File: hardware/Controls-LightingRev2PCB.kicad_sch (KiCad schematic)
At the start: 39 parts, among them IC2 TLV70433DBVT, J3 53307-2471, J4 Conn_02x08_Top_Bottom, Q2 IRLML0030, Q3 IRLML0030, U1 TLV2371DBV, U2 INA241A5xD, U3 INA241A5xD, U4 INA241A5xD, U5 SN74LV1T34DBV, U8 TLV2371DBV, U9 TLV2371DBV

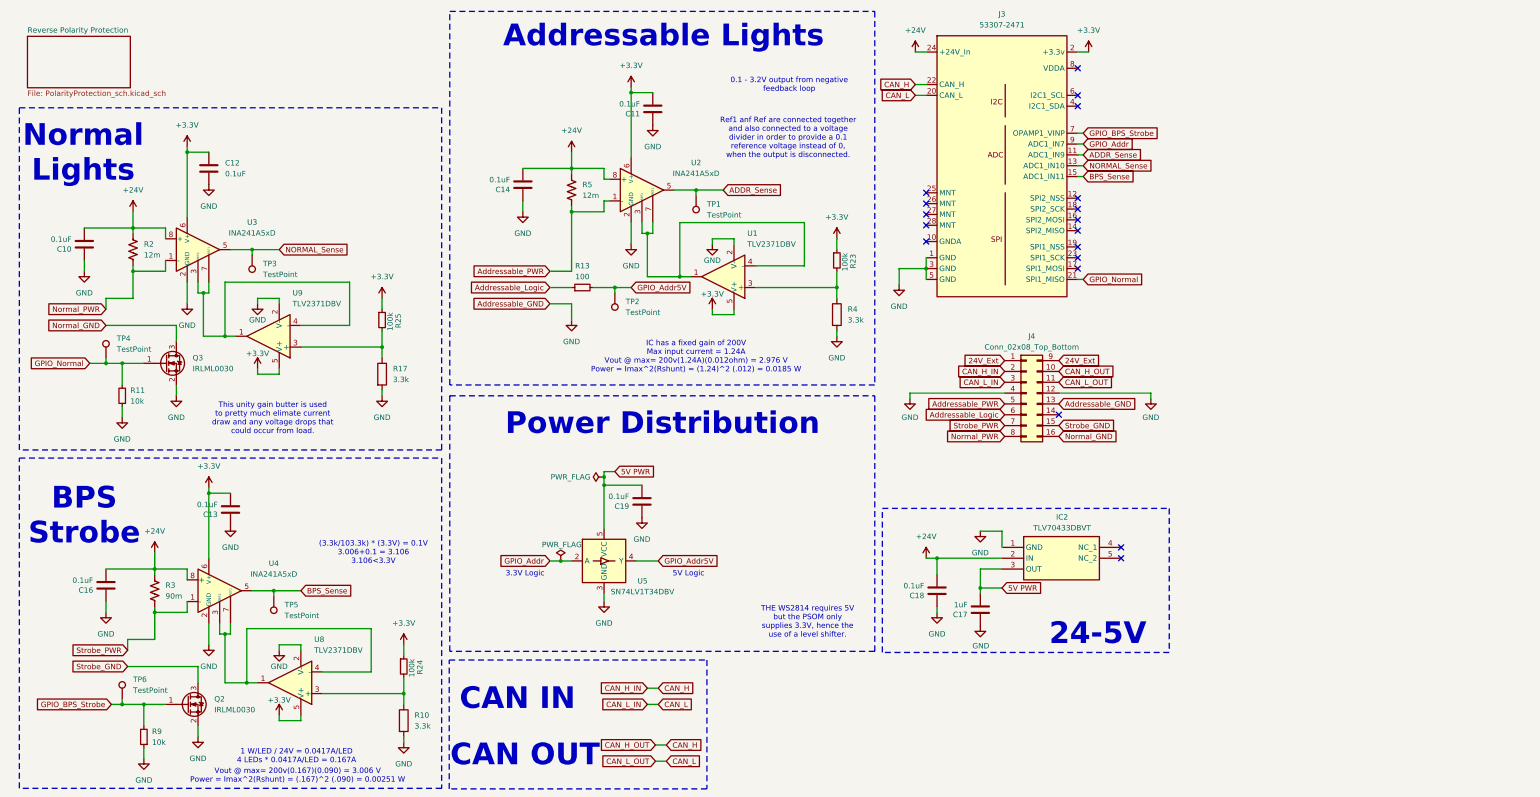
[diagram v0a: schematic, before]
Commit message: Routed but having issues with gnd being pretty isolated
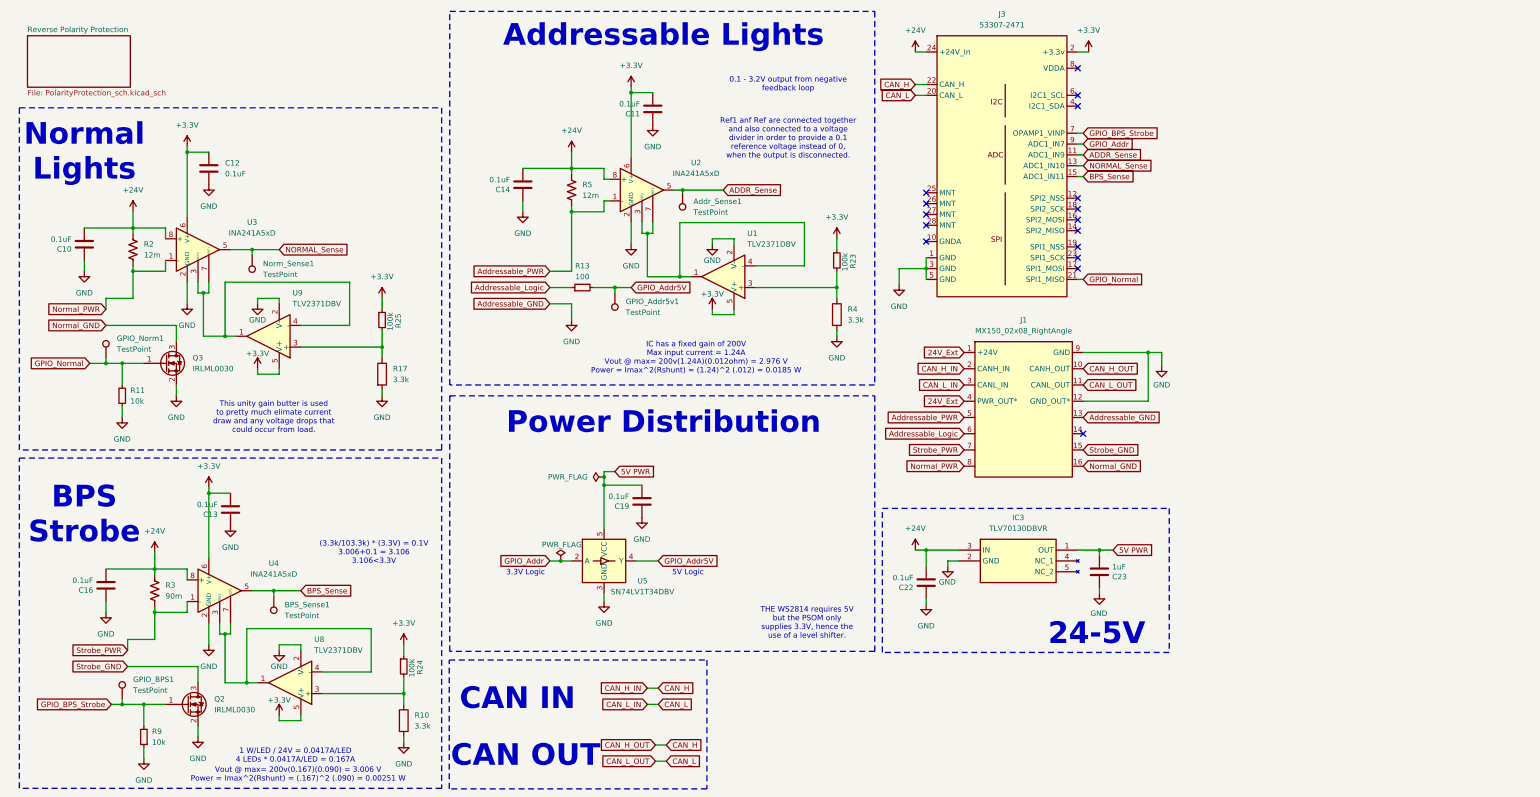
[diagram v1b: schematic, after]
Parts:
- removed C17: 1uF, Capacitor_SMD:C_0603_1608Metric, symbol Device:C
- removed C18: 0.1uF, Capacitor_SMD:C_0603_1608Metric, symbol Device:C
- removed IC2: TLV70433DBVT, SOT95P280X145-5N, symbol Misc:TLV70433DBVT
- removed J4: Conn_02x08_Top_Bottom, MX150:CONN_SD-75900-001_2X08_MOL, symbol Connector_Generic:Conn_02x08_Top_Bottom
- added C22: 0.1uF, Capacitor_SMD:C_0603_1608Metric, symbol Device:C
- added C23: 1uF, Capacitor_SMD:C_0603_1608Metric, symbol Device:C
- added IC3: TLV70130DBVR, UTSVT_Power:TLV70130DBVR, symbol UTSVT-Power:TLV70130DBVR
- added J1: MX150_02x08_RightAngle, UTSVT_Connectors:CONN_SD-75900-001_2X08_MOL, symbol UTSVT-Connectors:MX150_02x08_RightAngle
- R2, R3, R5: footprint Resistor_SMD:R_0603_1608Metric -> Resistor_SMD:R_1206_3216Metric_Pad1.30x1.75mm_HandSolder
- renumbered TP1 to Addr_Sense1, TP5 to BPS_Sense1, TP2 to GPIO_Addr5v1, TP6 to GPIO_BPS1, TP4 to GPIO_Norm1, TP3 to Norm_Sense1
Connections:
- net +24V: now also C22.2, IC3.3 (IN)
- net 24V_Ext: now also J1.1 (+24V), J1.4 (PWR_OUT*)
- net 5V PWR: now also C23.2, IC3.1 (OUT)
- net Addressable_Logic: now also J1.6
- net Addressable_PWR: now also J1.5
- net CAN_H: now also J1.10 (CANH_OUT), J1.2 (CANH_IN)
- net CAN_L: now also J1.11 (CANL_OUT), J1.3 (CANL_IN)
- net GND: now also C22.1, C23.1, IC3.2 (GND), J1.12 (GND_OUT*), J1.13, J1.9 (GND)
- net Normal_GND: now also J1.16
- net Normal_PWR: now also J1.8
- net Strobe_GND: now also J1.15
- net Strobe_PWR: now also J1.7
- no-connect marks 18 -> 16
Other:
- moved on the sheet: Addr_Sense1

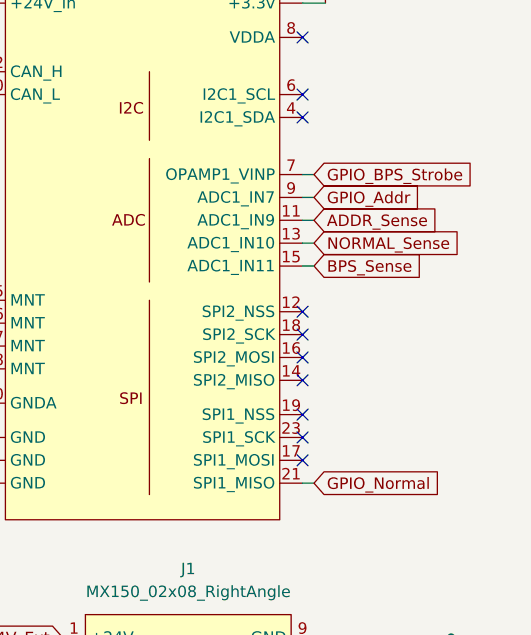
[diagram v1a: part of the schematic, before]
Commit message: Test points added
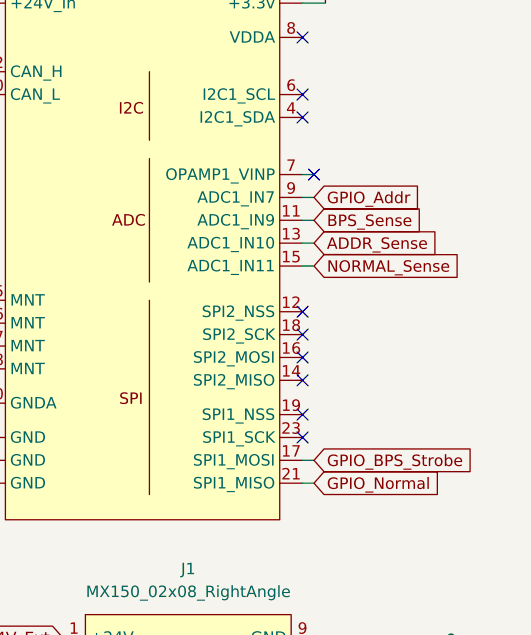
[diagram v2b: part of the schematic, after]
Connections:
- net ADDR_Sense: now also J3.13 (ADC1_IN10); no longer J3.11 (ADC1_IN9)
- net BPS_Sense: now also J3.11 (ADC1_IN9); no longer J3.15 (ADC1_IN11)
- net GPIO_BPS_Strobe: now also J3.17 (SPI1_MOSI); no longer J3.7 (OPAMP1_VINP)
- net NORMAL_Sense: now also J3.15 (ADC1_IN11); no longer J3.13 (ADC1_IN10)

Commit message: BOM
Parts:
- C12: P/N (none) -> MLASH168SB7104KTNA01
- C22: P/N MLASU168SB5105KTNA01 -> MLASH168SB7104KTNA01
- Q2, Q3: P/N (none) -> IRLML0030TRPBF
- R10, R17, R4: P/N (none) -> ERJ-S03D3301V
- R11, R9: P/N CRCW080510K0FKEAC -> CRCW060310K0FKEI
- R13: value 100 -> 100k; P/N SDR10EZPF1001 -> CRCW0603100KFKEE
- R2, R5: P/N (none) -> RLC73PV2ER012FTDF
- R23, R24, R25: P/N CRCW0805100KFKEAC -> CRCW0603100KFKEE
- R3: P/N (none) -> ERJ-L14UF90MU
- U1, U8, U9: P/N (none) -> TLV2371IDBVR
- U2, U3, U4: P/N (none) -> INA241A5QDRQ1
- U5: P/N (none) -> SN74LV1T34DBVR
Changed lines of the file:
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@@
 			)
 		)
-		(property "Description" ""
+		(property "Description" "Thick Film Resistors - SMD 100K OHM 1%"
 			(at 104.14 167.64 0)
 			(effects
@@
 			)
 		)
-		(property "P/N" "CRCW0805100KFKEAC"
+		(property "P/N" "CRCW0603100KFKEE"
 			(at 104.14 167.64 0)
 			(effects
@@
 			)
 		)
-		(property "Description" "Unpolarized capacitor"
+		(property "Description" "Multilayer Ceramic Capacitors MLCC - SMD/SMT 100V 0.1uF X7R 0603 10% Medical"
 			(at 132.08 54.61 0)
 			(effects
@@
 			)
 		)
-		(property "Description" "Unpolarized capacitor"
+		(property "Description" "Multilayer Ceramic Capacitors MLCC - SMD/SMT 100V 0.1uF X7R 0603 10% Medical"
 			(at 29.21 68.58 0)
 			(effects
@@
 			)
 		)
-		(property "Description" "Resistor"
+		(property "Description" "Thick Film Resistors - SMD 0603 0.5% 3.3kOhm Anti-Sulfur AEC-Q200"
 			(at 205.74 85.09 0)
 			(effects
@@
 			)
 		)
+		(property "P/N" "ERJ-S03D3301V"
+			(at 205.74 85.09 0)
+			(effects
+				(font
+					(size 1.27 1.27)
+				)
+			)
+		)
 		(pin "2"
 		)
@@
 			)
 		)
-		(property "Description" "Rail-to-Rail Input/Output Operational Amplifier, SOT-23-5"
+		(property "Description" "Operational Amplifiers - Op Amps 550uA/Ch 3MHz R/R Op A 595-TLV2371IDBVT"
 			(at 179.07 76.2 0)
 			(effects
@@
 			)
 		)
+		(property "P/N" "TLV2371IDBVR"
+			(at 179.07 76.2 0)
+			(effects
+				(font
+					(size 1.27 1.27)
+				)
+			)
+		)
 		(pin "5"
 		)
@@
 			)
 		)
-		(property "Description" ""
+		(property "Description" "Thick Film Resistors - SMD 10K OHM 1%"
 			(at 43.18 184.15 0)
 			(effects
@@
 			)
 		)
-		(property "P/N" "CRCW080510K0FKEAC"
+		(property "P/N" "CRCW060310K0FKEI "
 			(at 43.18 184.15 0)
 			(effects
@@
 			)
 		)
-		(property "Description" ""
+		(property "Description" "Thick Film Resistors - SMD 10K OHM 1%"
 			(at 38.1 104.14 0)
 			(effects
@@
 			)
 		)
-		(property "P/N" "CRCW080510K0FKEAC"
+		(property "P/N" "CRCW060310K0FKEI "
 			(at 38.1 104.14 0)
 			(effects
@@
 			)
 		)
-		(property "Description" "Unpolarized capacitor"
+		(property "Description" "Multilayer Ceramic Capacitors MLCC - SMD/SMT 100V 0.1uF X7R 0603 10% Medical"
 			(at 162.56 36.83 0)
 			(effects
@@
 			)
 		)
-		(property "Description" "Unpolarized capacitor"
+		(property "Description" "Multilayer Ceramic Capacitors MLCC - SMD/SMT 100V 0.1uF X7R 0603 10% Medical"
 			(at 226.695 147.955 0)
 			(effects
@@
 			)
 		)
-		(property "P/N" "MLASU168SB5105KTNA01"
+		(property "P/N" "MLASH168SB7104KTNA01"
 			(at 226.695 147.955 0)
 			(effects
@@
 			)
 		)
-		(property "Description" "Unpolarized capacitor"
+		(property "Description" "Multilayer Ceramic Capacitors MLCC - SMD/SMT 50V 1uF X5R 0603 10%"
 			(at 267.335 145.415 0)
 			(effects
@@
 			)
 		)
-		(property "Description" "Resistor, US symbol"
+		(property "Description" "Current Sense Resistors - SMD 1210 90mOhm 1% Curr Sense AEC-Q200"
 			(at 45.72 149.86 0)
 			(effects
@@
 			)
 		)
+		(property "P/N" "ERJ-L14UF90MU"
+			(at 45.72 149.86 0)
+			(effects
+				(font
+					(size 1.27 1.27)
+				)
+			)
+		)
 		(pin "1"
 		)
@@
 			)
 		)
-		(property "Value" "100"
+		(property "Value" "100k"
 			(at 146.05 76.2 90)
 			(effects
@@
 			)
 		)
-		(property "Description" ""
+		(property "Description" "Thick Film Resistors - SMD 100K OHM 1%"
 			(at 146.05 78.74 0)
 			(effects
@@
 			)
 		)
-		(property "P/N" "SDR10EZPF1001"
+		(property "P/N" "CRCW0603100KFKEE"
 			(at 146.05 78.74 0)
 			(effects
@@
 			)
 		)
-		(property "Description" "Resistor"
+		(property "Description" "Thick Film Resistors - SMD 0603 0.5% 3.3kOhm Anti-Sulfur AEC-Q200"
 			(at 99.06 99.06 0)
 			(effects
@@
 			)
 		)
+		(property "P/N" "ERJ-S03D3301V"
+			(at 99.06 99.06 0)
+			(effects
+				(font
+					(size 1.27 1.27)
+				)
+			)
+		)
 		(pin "2"
 		)
@@
 			)
 		)
-		(property "Description" "5.3A Id, 30V Vds, 27mOhm Rds, N-Channel HEXFET Power MOSFET, SOT-23"
+		(property "Description" "MOSFETs MOSFT 30V 5.2A 28mOhm 3.6nC Qg"
 			(at 48.26 96.52 0)
 			(effects
@@
 			)
 		)
+		(property "P/N" "IRLML0030TRPBF"
+			(at 48.26 96.52 0)
+			(effects
+				(font
+					(size 1.27 1.27)
+				)
+			)
+		)
 		(pin "1"
 		)
@@
 			)
 		)
-		(property "Description" ""
+		(property "Description" "Thick Film Resistors - SMD 100K OHM 1%"
 			(at 99.06 86.36 0)
 			(effects
@@
 			)
 		)
-		(property "P/N" "CRCW0805100KFKEAC"
+		(property "P/N" "CRCW0603100KFKEE"
 			(at 99.06 86.36 0)
 			(effects
@@
 			)
 		)
-		(property "Description" "Resistor, US symbol"
+		(property "Description" "Current Sense Resistors - SMD RLC73PV 2E R012 1% 1K RL"
 			(at 40.64 69.85 0)
 			(effects
@@
 			)
 		)
+		(property "P/N" "RLC73PV2ER012FTDF"
+			(at 40.64 69.85 0)
+			(effects
+				(font
+					(size 1.27 1.27)
+				)
+			)
+		)
 		(pin "1"
 		)
@@
 			)
 		)
-		(property "Description" "Unpolarized capacitor"
+		(property "Description" "Multilayer Ceramic Capacitors MLCC - SMD/SMT 100V 0.1uF X7R 0603 10% Medical"
 			(at 34.29 148.59 0)
 			(effects
@@
 			)
 		)
-		(property "Description" "Resistor, US symbol"
+		(property "Description" "Current Sense Resistors - SMD RLC73PV 2E R012 1% 1K RL"
 			(at 143.51 55.88 0)
 			(effects
@@
 			)
 		)
+		(property "P/N" "RLC73PV2ER012FTDF"
+			(at 143.51 55.88 0)
+			(effects
+				(font
+					(size 1.27 1.27)
+				)
+			)
+		)
 		(pin "1"
 		)
@@
 			)
 		)
-		(property "Description" ""
+		(property "Description" "Thick Film Resistors - SMD 100K OHM 1%"
 			(at 205.74 72.39 0)
 			(effects
@@
 			)
 		)
-		(property "P/N" "CRCW0805100KFKEAC"
+		(property "P/N" "CRCW0603100KFKEE"
 			(at 205.74 72.39 0)
 			(effects
@@
 			)
 		)
-		(property "Description" "Unpolarized capacitor"
+		(property "Description" "Multilayer Ceramic Capacitors MLCC - SMD/SMT 100V 0.1uF X7R 0603 10% Medical"
 			(at 160.02 128.905 0)
 			(effects
@@
 			)
 		)
-		(property "Description" "Rail-to-Rail Input/Output Operational Amplifier, SOT-23-5"
+		(property "Description" "Operational Amplifiers - Op Amps 550uA/Ch 3MHz R/R Op A 595-TLV2371IDBVT"
 			(at 77.47 171.45 0)
 			(effects
@@
 			)
 		)
+		(property "P/N" "TLV2371IDBVR"
+			(at 77.47 171.45 0)
+			(effects
+				(font
+					(size 1.27 1.27)
+				)
+			)
+		)
 		(pin "5"
 		)
@@
 			)
 		)
-		(property "Description" "High- and Low-Side, Bidirectional, Zero-Drift, Current-Sense Amplifier With Enhanced PWM Rejection, 200V/V, ±0.01% Gain Accuracy, ±10 μV Offset Voltage, SOIC-8"
+		(property "Description" "Current Sense Amplifiers AEC-Q100 -4V to 110 V bidirectional ultr"
 			(at 160.02 55.88 0)
 			(effects
@@
 			)
 		)
+		(property "P/N" "INA241A5QDRQ1"
+			(at 160.02 55.88 0)
+			(effects
+				(font
+					(size 1.27 1.27)
+				)
+			)
+		)
 		(pin "1"
 		)
@@
 			)
 		)
-		(property "Description" "Unpolarized capacitor"
+		(property "Description" "Multilayer Ceramic Capacitors MLCC - SMD/SMT 100V 0.1uF X7R 0603 10% Medical"
 			(at 63.5 130.81 0)
 			(effects
@@
 			)
 		)
-		(property "Description" "Single Power Supply, Single Buffer GATE, CMOS Logic, Level Shifter, SOT-23-5"
+		(property "Description" "Translation - Voltage Levels SGL Pwr Spply Buffer GATE CMOS"
 			(at 151.13 142.875 0)
 			(effects
@@
 			)
 		)
+		(property "P/N" "SN74LV1T34DBVR"
+			(at 151.13 142.875 0)
+			(effects
+				(font
+					(size 1.27 1.27)
+				)
+			)
+		)
 		(pin "2"
 		)
@@
 			)
 		)
-		(property "Description" "Unpolarized capacitor"
+		(property "Description" "Multilayer Ceramic Capacitors MLCC - SMD/SMT 100V 0.1uF X7R 0603 10% Medical"
 			(at 58.42 50.8 0)
 			(effects
@@
 			)
 		)
+		(property "P/N" "MLASH168SB7104KTNA01"
+			(at 58.42 50.8 0)
+			(effects
+				(font
+					(size 1.27 1.27)
+				)
+			)
+		)
 		(pin "1"
 		)
@@
 			)
 		)
-		(property "Description" "High- and Low-Side, Bidirectional, Zero-Drift, Current-Sense Amplifier With Enhanced PWM Rejection, 200V/V, ±0.01% Gain Accuracy, ±10 μV Offset Voltage, SOIC-8"
+		(property "Description" "Current Sense Amplifiers AEC-Q100 -4V to 110 V bidirectional ultr"
 			(at 55.88 69.85 0)
 			(effects
@@
 			)
 		)
+		(property "P/N" "INA241A5QDRQ1"
+			(at 55.88 69.85 0)
+			(effects
+				(font
+					(size 1.27 1.27)
+				)
+			)
+		)
 		(pin "1"
 		)
@@
 			)
 		)
-		(property "Description" "High- and Low-Side, Bidirectional, Zero-Drift, Current-Sense Amplifier With Enhanced PWM Rejection, 200V/V, ±0.01% Gain Accuracy, ±10 μV Offset Voltage, SOIC-8"
+		(property "Description" "Current Sense Amplifiers AEC-Q100 -4V to 110 V bidirectional ultr"
 			(at 60.96 149.86 0)
 			(effects
@@
 			)
 		)
+		(property "P/N" "INA241A5QDRQ1"
+			(at 60.96 149.86 0)
+			(effects
+				(font
+					(size 1.27 1.27)
+				)
+			)
+		)
 		(pin "1"
 		)
@@
 			)
 		)
-		(property "Description" "Rail-to-Rail Input/Output Operational Amplifier, SOT-23-5"
+		(property "Description" "Operational Amplifiers - Op Amps 550uA/Ch 3MHz R/R Op A 595-TLV2371IDBVT"
 			(at 72.39 90.17 0)
 			(effects
@@
 			)
 		)
+		(property "P/N" "TLV2371IDBVR"
+			(at 72.39 90.17 0)
+			(effects
+				(font
+					(size 1.27 1.27)
+				)
+			)
+		)
 		(pin "5"
 		)
@@
 			)
 		)
-		(property "Description" "5.3A Id, 30V Vds, 27mOhm Rds, N-Channel HEXFET Power MOSFET, SOT-23"
+		(property "Description" "MOSFETs MOSFT 30V 5.2A 28mOhm 3.6nC Qg"
 			(at 53.34 176.53 0)
 			(effects
@@
 			)
 		)
+		(property "P/N" "IRLML0030TRPBF"
+			(at 53.34 176.53 0)
+			(effects
+				(font
+					(size 1.27 1.27)
+				)
+			)
+		)
 		(pin "1"
 		)
@@
 			)
 		)
-		(property "Description" "Resistor"
+		(property "Description" "Thick Film Resistors - SMD 0603 0.5% 3.3kOhm Anti-Sulfur AEC-Q200"
 			(at 104.14 180.34 0)
 			(effects
@@
 			)
 		)
+		(property "P/N" "ERJ-S03D3301V"
+			(at 104.14 180.34 0)
+			(effects
+				(font
+					(size 1.27 1.27)
+				)
+			)
+		)

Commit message: RevA
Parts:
- removed J1: MX150_02x08_RightAngle, UTSVT_Connectors:CONN_SD-75900-001_2X08_MOL, symbol UTSVT-Connectors:MX150_02x08_RightAngle
- added J2: MX150_02x08_RightAngle, UTSVT_Connectors:MX150_02x08_RightAngle, symbol UTSVT-Connectors:MX150_02x08_RightAngle
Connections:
- net 24V_Ext: now also J2.1 (+24V), J2.4 (PWR_OUT*)
- net Addressable_Logic: now also J2.6
- net Addressable_PWR: now also J2.5
- net CAN_H: now also J2.10 (CANH_OUT), J2.2 (CANH_IN)
- net CAN_L: now also J2.11 (CANL_OUT), J2.3 (CANL_IN)
- net GND: now also J2.12 (GND_OUT*), J2.13, J2.9 (GND)
- net Normal_GND: now also J2.16
- net Normal_PWR: now also J2.8
- net Strobe_GND: now also J2.15
- net Strobe_PWR: now also J2.7

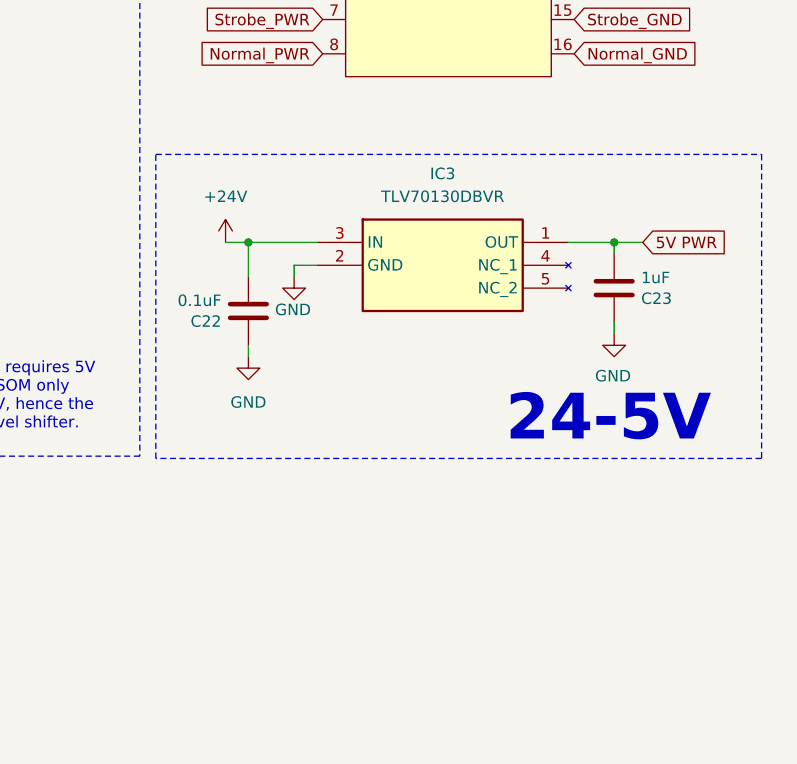
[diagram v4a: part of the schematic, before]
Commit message: Correct LDO
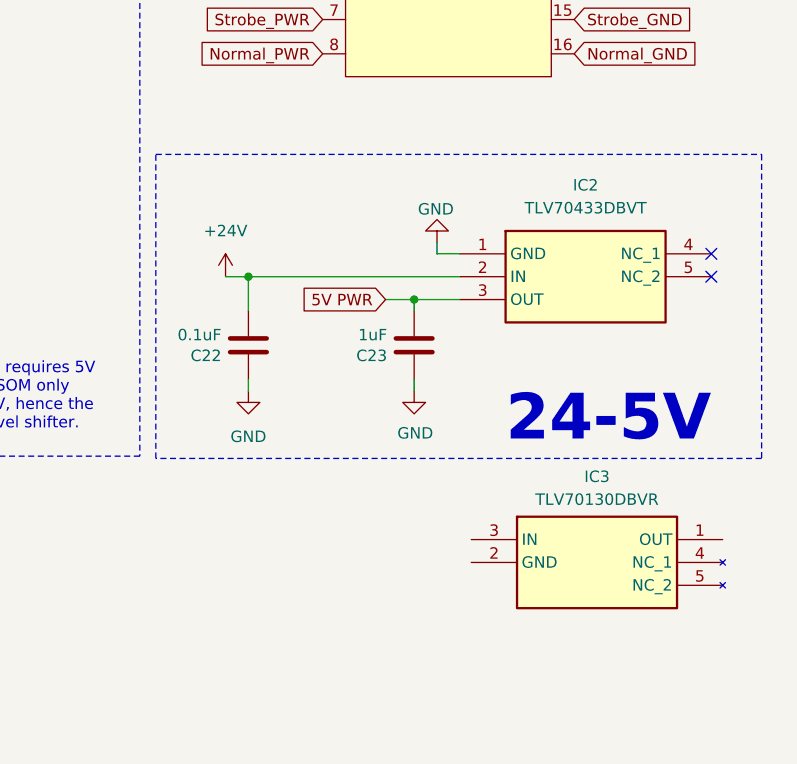
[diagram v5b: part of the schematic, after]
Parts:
- added IC2: TLV70433DBVT, SOT95P280X145-5N, symbol TLB70433DBVT:TLV70433DBVT
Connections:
- net +24V: now also IC2.2 (IN); no longer IC3.3 (IN)
- net 5V PWR: now also IC2.3 (OUT); no longer IC3.1 (OUT)
- net GND: now also IC2.1 (GND); no longer IC3.2 (GND)
- no-connect marks 16 -> 18
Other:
- moved on the sheet: C22, C23
